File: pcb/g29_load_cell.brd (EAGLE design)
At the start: 64.4 x 38.1 mm, 6 parts, among them IC1 INA122P

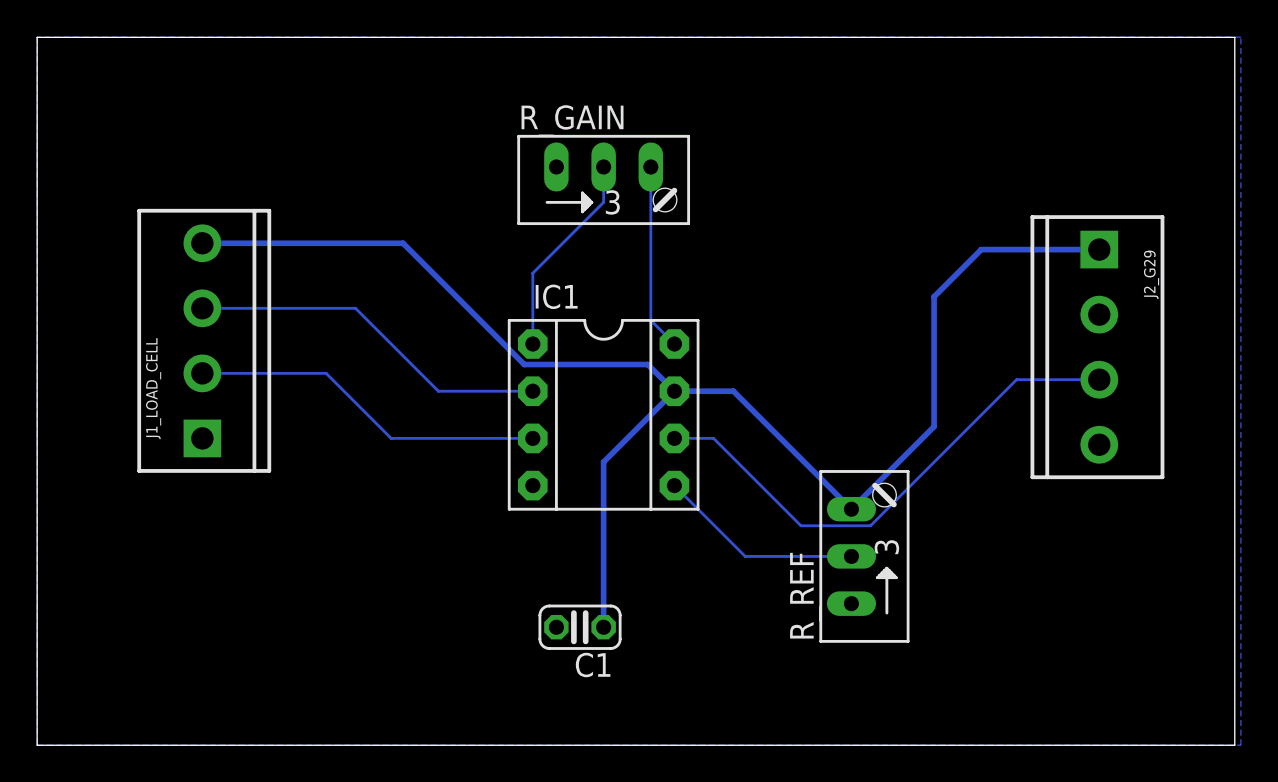
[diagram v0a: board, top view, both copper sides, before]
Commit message: fixed ERC errors
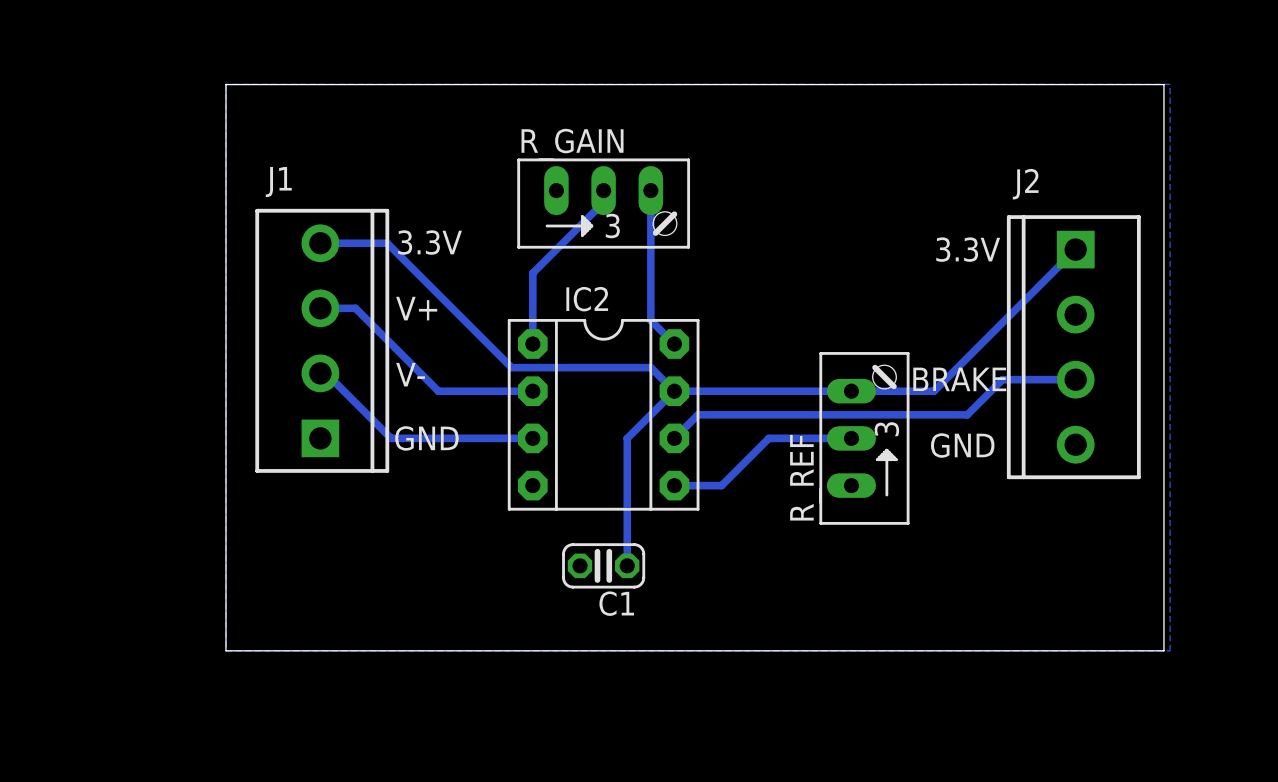
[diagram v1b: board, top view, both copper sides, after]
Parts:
- removed IC1: INA122P, burr-brown:DIL08
- removed J1_LOAD_CELL, J2_G29: (no value), SparkFun-Connectors:SCREWTERMINAL-3.5MM-4
- added IC2: INA122P, g29_load_cell:DIL08
- added J1: LOAD_CELL, SparkFun-Connectors:SCREWTERMINAL-3.5MM-4
- added J2: G29, SparkFun-Connectors:SCREWTERMINAL-3.5MM-4
- moved R_REF 6.35 mm to (59.7, 40.6)
- moved C1 3.54 mm to (45.7, 33.8)
- moved R_GAIN 1.27 mm to (45.7, 53.3)
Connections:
- net 3.3V: now also IC2.7, J1.4, J2.1; no longer IC1.7, J1_LOAD_CELL.4, J2_G29.1
- net GND: now also IC2.4, J1.1, J2.4; no longer IC1.4, J1_LOAD_CELL.1, J2_G29.4
- net N$1: now also IC2.8; no longer IC1.8
- net N$2: now also IC2.1; no longer IC1.1
- net N$3: now also IC2.3, J1.2; no longer IC1.3, J1_LOAD_CELL.2
- net N$4: now also IC2.2, J1.3; no longer IC1.2, J1_LOAD_CELL.3
- net N$6: now also IC2.5; no longer IC1.5
- net N$7: now also IC2.6, J2.3; no longer IC1.6, J2_G29.3
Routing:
- net 3.3V: track 78.3 -> 57.5 mm
- net N$3: track 19.2 -> 12.9 mm
- net N$4: track 19.6 -> 13.3 mm
- net N$7: track 28.1 -> 22.9 mm
- net N$2: track 11.1 -> 9.83 mm
- net N$1: track 10.1 -> 8.78 mm
- net N$6: track 11.1 -> 10.6 mm
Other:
- board size 64.4 x 38.1 mm -> 50.5 x 30.5 mm
- board text added: "3.3V"
- board text added: "BRAKE"
- board text added: "GND"
- board text added: "V+"
- board text added: "V-"
